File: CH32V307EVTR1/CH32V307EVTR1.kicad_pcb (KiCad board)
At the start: 2 copper layers, 74 x 82.6 mm, 2 parts, among them J1 Conn_02x27_Odd_Even, J2 Conn_02x27_Odd_Even

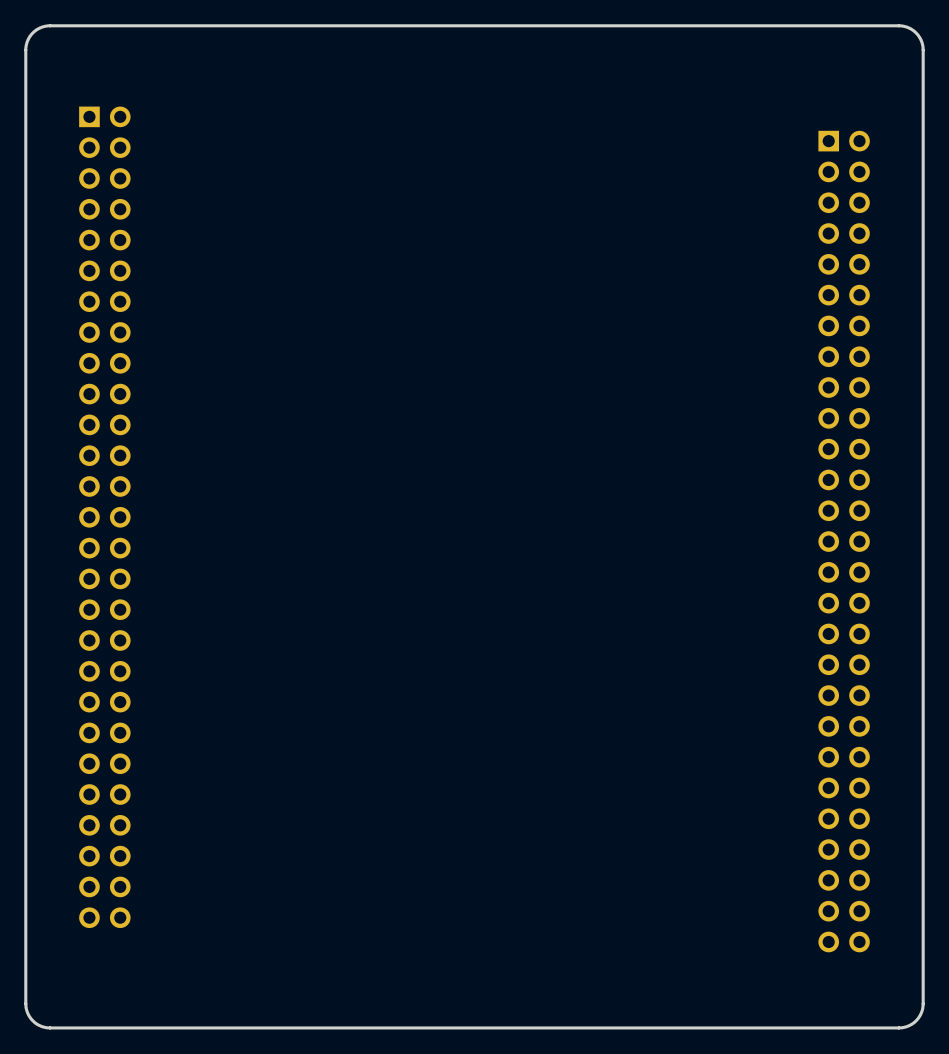
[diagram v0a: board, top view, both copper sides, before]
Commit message: Define the Edge and minimal footprints positions in CH32V307 template.
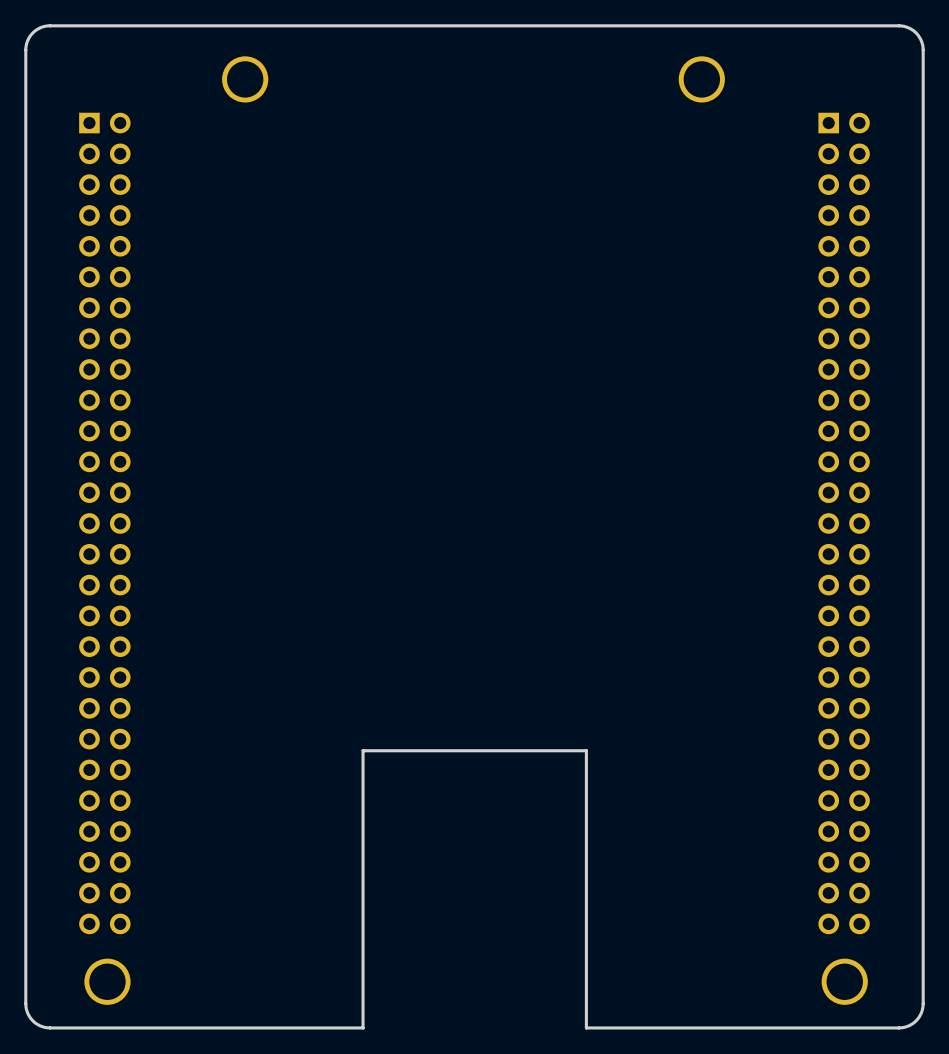
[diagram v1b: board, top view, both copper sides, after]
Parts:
- added REF**: MountingHole_3mm_Pad, MountingHole:MountingHole_3mm_Pad, F.Cu at (57.5, 148.6)
- added REF**: MountingHole_3mm_Pad, MountingHole:MountingHole_3mm_Pad, F.Cu at (106.5, 74.2)
- added REF**: MountingHole_3mm_Pad, MountingHole:MountingHole_3mm_Pad, F.Cu at (68.9, 74.2)
- added REF**: MountingHole_3mm_Pad, MountingHole:MountingHole_3mm_Pad, F.Cu at (118.3, 148.6)
- moved J2 1.49 mm to (117.0, 77.8)
- moved J1 0.51 mm to (56.0, 77.8)
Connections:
- J1 pad 1: unconnected-(J1-Pin_1-Pad1) -> VCC
- J1 pad 11: unconnected-(J1-Pin_11-Pad11) -> ELED1
- J1 pad 12: unconnected-(J1-Pin_12-Pad12) -> VCC
- J1 pad 13: unconnected-(J1-Pin_13-Pad13) -> ELED2
- J1 pad 14: unconnected-(J1-Pin_14-Pad14) -> NRST
- J1 pad 15: unconnected-(J1-Pin_15-Pad15) -> VCC
- J1 pad 16: unconnected-(J1-Pin_16-Pad16) -> VCC
- J1 pad 17: unconnected-(J1-Pin_17-Pad17) -> 5V
- J1 pad 18: unconnected-(J1-Pin_18-Pad18) -> 5V
- J1 pad 19: unconnected-(J1-Pin_19-Pad19) -> LED1
- J1 pad 2: unconnected-(J1-Pin_2-Pad2) -> VCC
- J1 pad 20: unconnected-(J1-Pin_20-Pad20) -> GND
- J1 pad 21: unconnected-(J1-Pin_21-Pad21) -> LED2
- J1 pad 22: unconnected-(J1-Pin_22-Pad22) -> GND
- J1 pad 23: unconnected-(J1-Pin_23-Pad23) -> PC0
- J1 pad 24: unconnected-(J1-Pin_24-Pad24) -> 5V
- J1 pad 25: unconnected-(J1-Pin_25-Pad25) -> GND
- J1 pad 26: unconnected-(J1-Pin_26-Pad26) -> GND
- J1 pad 27: unconnected-(J1-Pin_27-Pad27) -> PA14
- J1 pad 28: unconnected-(J1-Pin_28-Pad28) -> PA0
- J1 pad 29: unconnected-(J1-Pin_29-Pad29) -> PA13
- J1 pad 3: unconnected-(J1-Pin_3-Pad3) -> VCC
- J1 pad 30: unconnected-(J1-Pin_30-Pad30) -> PA1
- J1 pad 31: unconnected-(J1-Pin_31-Pad31) -> KEY
- J1 pad 32: unconnected-(J1-Pin_32-Pad32) -> PA2
- J1 pad 33: unconnected-(J1-Pin_33-Pad33) -> PC1
- J1 pad 34: unconnected-(J1-Pin_34-Pad34) -> PA3
- J1 pad 35: unconnected-(J1-Pin_35-Pad35) -> PC2
- J1 pad 36: unconnected-(J1-Pin_36-Pad36) -> PA4
- J1 pad 37: unconnected-(J1-Pin_37-Pad37) -> PC3
- J1 pad 38: unconnected-(J1-Pin_38-Pad38) -> PA5
- J1 pad 39: unconnected-(J1-Pin_39-Pad39) -> PC4
- J1 pad 4: unconnected-(J1-Pin_4-Pad4) -> VCC
- J1 pad 40: unconnected-(J1-Pin_40-Pad40) -> PC5
- J1 pad 41: unconnected-(J1-Pin_41-Pad41) -> PB2
- J1 pad 42: unconnected-(J1-Pin_42-Pad42) -> PE7
- J1 pad 43: unconnected-(J1-Pin_43-Pad43) -> PE8
- J1 pad 44: unconnected-(J1-Pin_44-Pad44) -> PE9
- J1 pad 45: unconnected-(J1-Pin_45-Pad45) -> PE10
- J1 pad 46: unconnected-(J1-Pin_46-Pad46) -> PE11
- J1 pad 47: unconnected-(J1-Pin_47-Pad47) -> PE12
- J1 pad 48: unconnected-(J1-Pin_48-Pad48) -> PE13
- J1 pad 49: unconnected-(J1-Pin_49-Pad49) -> PE14
- J1 pad 5: unconnected-(J1-Pin_5-Pad5) -> Boot1
- J1 pad 50: unconnected-(J1-Pin_50-Pad50) -> PE15
- J1 pad 51: unconnected-(J1-Pin_51-Pad51) -> PD8
- J1 pad 52: unconnected-(J1-Pin_52-Pad52) -> PD9
- J1 pad 53: unconnected-(J1-Pin_53-Pad53) -> PD10
- J1 pad 54: unconnected-(J1-Pin_54-Pad54) -> PD11
- J1 pad 6: unconnected-(J1-Pin_6-Pad6) -> Boot0
- J1 pad 7: unconnected-(J1-Pin_7-Pad7) -> GND
- J1 pad 8: unconnected-(J1-Pin_8-Pad8) -> GND
- J1 pad 9: unconnected-(J1-Pin_9-Pad9) -> GND
- J2 pad 1: unconnected-(J2-Pin_1-Pad1) -> PB10
- J2 pad 10: unconnected-(J2-Pin_10-Pad10) -> PE4
- J2 pad 11: unconnected-(J2-Pin_11-Pad11) -> PB14
- J2 pad 12: unconnected-(J2-Pin_12-Pad12) -> PE3
- J2 pad 13: unconnected-(J2-Pin_13-Pad13) -> PB15
- J2 pad 14: unconnected-(J2-Pin_14-Pad14) -> PE2
- J2 pad 15: unconnected-(J2-Pin_15-Pad15) -> PB0
- J2 pad 16: unconnected-(J2-Pin_16-Pad16) -> PE1
- J2 pad 17: unconnected-(J2-Pin_17-Pad17) -> PB0
- J2 pad 18: unconnected-(J2-Pin_18-Pad18) -> PE0
- J2 pad 19: unconnected-(J2-Pin_19-Pad19) -> PB1
- J2 pad 2: unconnected-(J2-Pin_2-Pad2) -> PC13
- J2 pad 20: unconnected-(J2-Pin_20-Pad20) -> PB7
- J2 pad 21: unconnected-(J2-Pin_21-Pad21) -> PD6
- J2 pad 22: unconnected-(J2-Pin_22-Pad22) -> PB6
- J2 pad 23: unconnected-(J2-Pin_23-Pad23) -> PB9
- J2 pad 24: unconnected-(J2-Pin_24-Pad24) -> PB4
- J2 pad 25: unconnected-(J2-Pin_25-Pad25) -> PB8
- J2 pad 26: unconnected-(J2-Pin_26-Pad26) -> PB3
- J2 pad 27: unconnected-(J2-Pin_27-Pad27) -> PB5
- J2 pad 28: unconnected-(J2-Pin_28-Pad28) -> PD7
- J2 pad 29: unconnected-(J2-Pin_29-Pad29) -> PA6
- J2 pad 3: unconnected-(J2-Pin_3-Pad3) -> PB11
- J2 pad 30: unconnected-(J2-Pin_30-Pad30) -> PD5
- J2 pad 31: unconnected-(J2-Pin_31-Pad31) -> PA7
- J2 pad 32: unconnected-(J2-Pin_32-Pad32) -> PD4
- J2 pad 33: unconnected-(J2-Pin_33-Pad33) -> PA8
- J2 pad 34: unconnected-(J2-Pin_34-Pad34) -> PD3
- J2 pad 35: unconnected-(J2-Pin_35-Pad35) -> PA9
- J2 pad 36: unconnected-(J2-Pin_36-Pad36) -> PD2
- J2 pad 37: unconnected-(J2-Pin_37-Pad37) -> PA10
- J2 pad 38: unconnected-(J2-Pin_38-Pad38) -> PD1
- J2 pad 39: unconnected-(J2-Pin_39-Pad39) -> PD0
- J2 pad 4: unconnected-(J2-Pin_4-Pad4) -> VBAT
- J2 pad 40: unconnected-(J2-Pin_40-Pad40) -> PC12
- J2 pad 41: unconnected-(J2-Pin_41-Pad41) -> PC11
- J2 pad 42: unconnected-(J2-Pin_42-Pad42) -> PC10
- J2 pad 43: unconnected-(J2-Pin_43-Pad43) -> PA15
- J2 pad 44: unconnected-(J2-Pin_44-Pad44) -> VIO
- J2 pad 45: unconnected-(J2-Pin_45-Pad45) -> PA12
- J2 pad 46: unconnected-(J2-Pin_46-Pad46) -> PA11
- J2 pad 47: unconnected-(J2-Pin_47-Pad47) -> PC9
- J2 pad 48: unconnected-(J2-Pin_48-Pad48) -> PC8
- J2 pad 49: unconnected-(J2-Pin_49-Pad49) -> PC7
- J2 pad 5: unconnected-(J2-Pin_5-Pad5) -> VDDA
- J2 pad 50: unconnected-(J2-Pin_50-Pad50) -> PC6
- J2 pad 51: unconnected-(J2-Pin_51-Pad51) -> PD15
- J2 pad 52: unconnected-(J2-Pin_52-Pad52) -> PD14
- J2 pad 53: unconnected-(J2-Pin_53-Pad53) -> PD13
- J2 pad 54: unconnected-(J2-Pin_54-Pad54) -> PD12
- J2 pad 6: unconnected-(J2-Pin_6-Pad6) -> PE6
- J2 pad 7: unconnected-(J2-Pin_7-Pad7) -> GND
- J2 pad 8: unconnected-(J2-Pin_8-Pad8) -> PE5
- J2 pad 9: unconnected-(J2-Pin_9-Pad9) -> PB13
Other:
- outline, holes or cut-outs redrawn
- board text added: "Optional margin"
